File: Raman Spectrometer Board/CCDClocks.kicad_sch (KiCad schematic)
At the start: 0 parts

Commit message: CCD clock without teensy connect
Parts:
- added Q4, Q5: BSS138, Package_TO_SOT_SMD:SOT-23, symbol Transistor_FET:BSS138
- added R10, R8: 2.2k, symbol Device:R_US
- added R7, R9: 4.7k, symbol Device:R_US
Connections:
- new net: Q4.1 (G), R8.2
- new net: Q5.1 (G), R10.2
- new net +3V3: R10.1, R8.1
- new net +5V: R7.1, R9.1
- new net CCD_CLK_3V3: Q4.2 (S)
- new net CCD_CLK_5V: Q4.3 (D), R7.2
- new net CCD_ROG_3V3: Q5.2 (S)
- new net CCD_ROG_5V: Q5.3 (D), R9.2

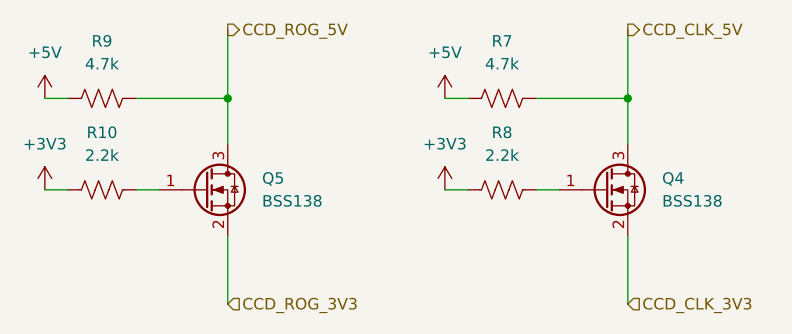
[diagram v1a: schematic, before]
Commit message: Labels change for clock pins
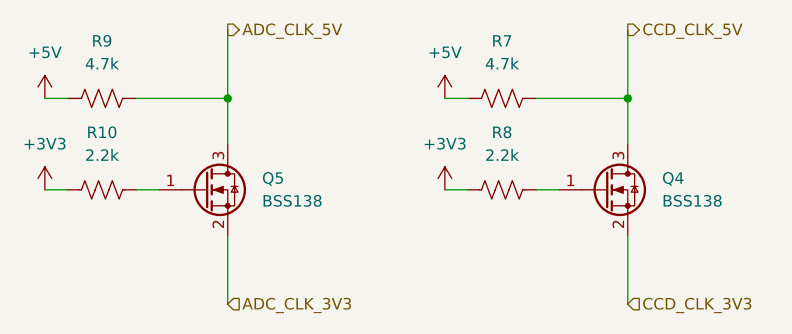
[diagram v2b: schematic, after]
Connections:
- net CCD_ROG_3V3 renamed ADC_CLK_3V3
- net CCD_ROG_5V renamed ADC_CLK_5V
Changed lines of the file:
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@@
 		)
 	)
-	(hierarchical_label "CCD_ROG_5V"
+	(hierarchical_label "ADC_CLK_5V"
 		(shape output)
 		(at 149.86 78.74 0)
@@
 		)
 	)
-	(hierarchical_label "CCD_ROG_3V3"
+	(hierarchical_label "ADC_CLK_3V3"
 		(shape input)
 		(at 149.86 109.22 0)

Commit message: Added footprints to main board
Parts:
- R10, R7, R8, R9: footprint (none) -> Resistor_SMD:R_0201_0603Metric_Pad0.64x0.40mm_HandSolder
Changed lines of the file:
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@@
 			)
 		)
-		(property "Footprint" ""
+		(property "Footprint" "Resistor_SMD:R_0201_0603Metric_Pad0.64x0.40mm_HandSolder"
 			(at 180.594 85.344 90)
 			(effects
@@
 			)
 		)
-		(property "Footprint" ""
+		(property "Footprint" "Resistor_SMD:R_0201_0603Metric_Pad0.64x0.40mm_HandSolder"
 			(at 180.594 95.504 90)
 			(effects
@@
 			)
 		)
-		(property "Footprint" ""
+		(property "Footprint" "Resistor_SMD:R_0201_0603Metric_Pad0.64x0.40mm_HandSolder"
 			(at 136.144 85.344 90)
 			(effects
@@
 			)
 		)
-		(property "Footprint" ""
+		(property "Footprint" "Resistor_SMD:R_0201_0603Metric_Pad0.64x0.40mm_HandSolder"
 			(at 136.144 95.504 90)
 			(effects

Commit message: tof voltages connected
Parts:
- R10, R7, R8, R9: footprint Resistor_SMD:R_0201_0603Metric_Pad0.64x0.40mm_HandSolder -> (none)
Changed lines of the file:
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@@
 			)
 		)
-		(property "Footprint" "Resistor_SMD:R_0201_0603Metric_Pad0.64x0.40mm_HandSolder"
+		(property "Footprint" ""
 			(at 180.594 85.344 90)
 			(effects
@@
 			)
 		)
-		(property "Footprint" "Resistor_SMD:R_0201_0603Metric_Pad0.64x0.40mm_HandSolder"
+		(property "Footprint" ""
 			(at 180.594 95.504 90)
 			(effects
@@
 			)
 		)
-		(property "Footprint" "Resistor_SMD:R_0201_0603Metric_Pad0.64x0.40mm_HandSolder"
+		(property "Footprint" ""
 			(at 136.144 85.344 90)
 			(effects
@@
 			)
 		)
-		(property "Footprint" "Resistor_SMD:R_0201_0603Metric_Pad0.64x0.40mm_HandSolder"
+		(property "Footprint" ""
 			(at 136.144 95.504 90)
 			(effects
